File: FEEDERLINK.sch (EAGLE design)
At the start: 5 parts, among them J5 M02X5-SHROUDED

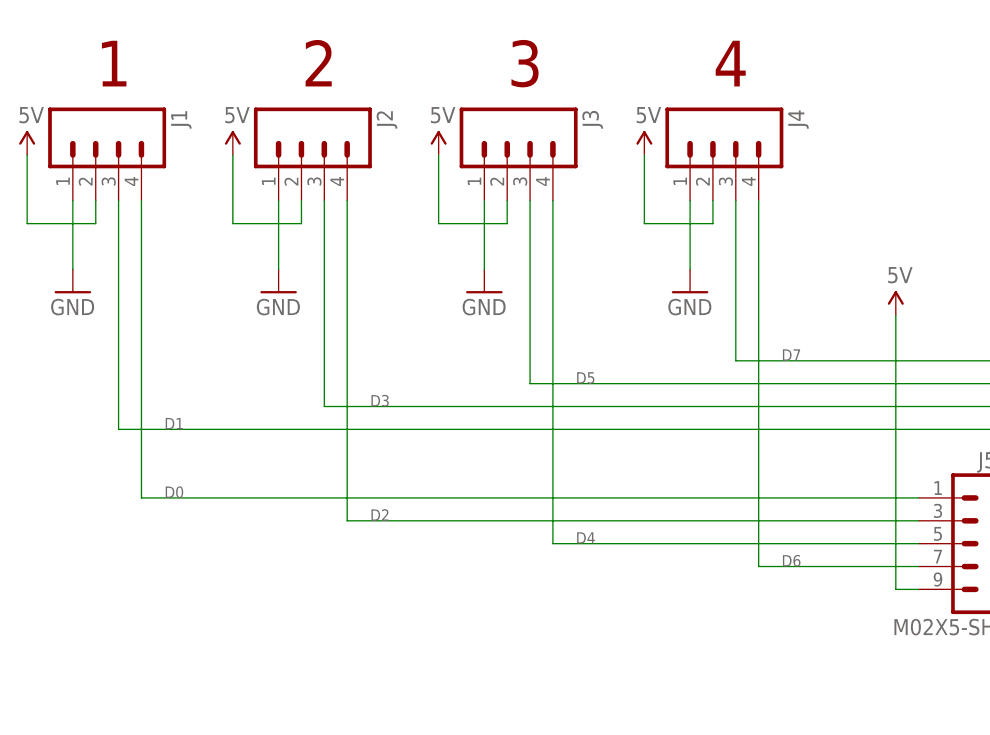
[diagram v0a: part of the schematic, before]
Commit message: Changed net names to match functions
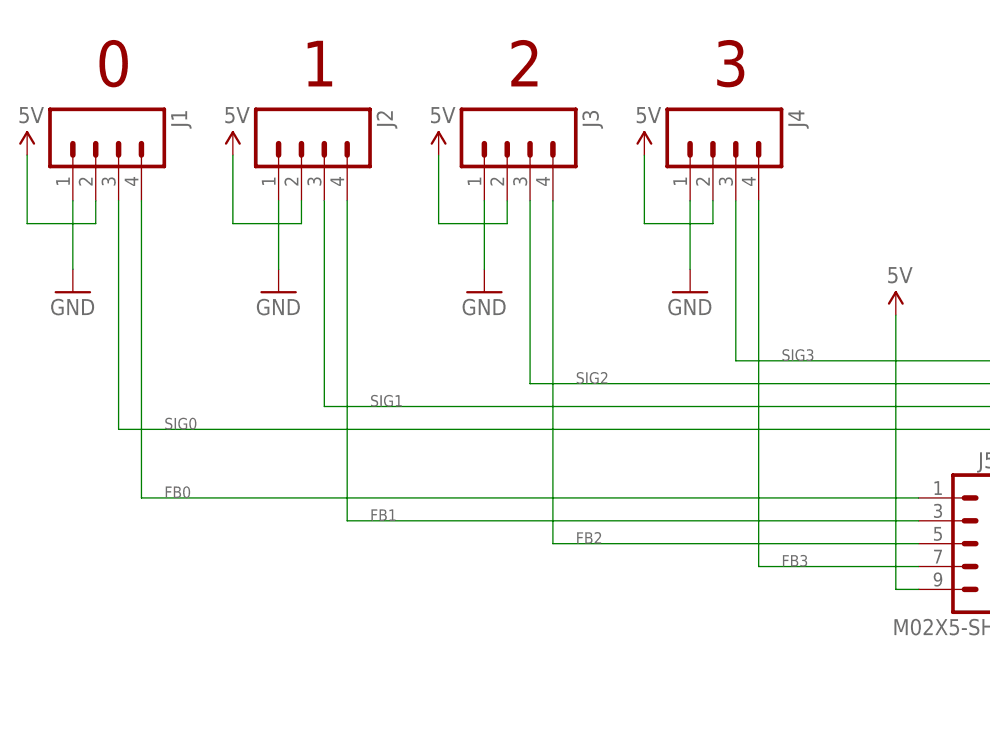
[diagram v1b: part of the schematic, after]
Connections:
- net D0 renamed FB0
- net D1 renamed SIG0
- net D2 renamed FB1
- net D3 renamed SIG1
- net D4 renamed FB2
- net D5 renamed SIG2
- net D6 renamed FB3
- net D7 renamed SIG3
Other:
- note added: "0"
- note removed: "4"
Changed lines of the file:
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@@
 <text x="134.366" y="6.35" size="1.778" layer="94">Released under the TAPR Open Hardware License: www.tapr.org/ohl</text>
 <text x="197.866" y="14.478" size="1.778" layer="94">www.superhouse.tv/fl</text>
-<text x="68.58" y="124.46" size="5.08" layer="94" ratio="12">1</text>
-<text x="91.44" y="124.46" size="5.08" layer="94" ratio="12">2</text>
-<text x="114.3" y="124.46" size="5.08" layer="94" ratio="12">3</text>
-<text x="137.16" y="124.46" size="5.08" layer="94" ratio="12">4</text>
+<text x="68.58" y="124.46" size="5.08" layer="94" ratio="12">0</text>
+<text x="91.44" y="124.46" size="5.08" layer="94" ratio="12">1</text>
+<text x="114.3" y="124.46" size="5.08" layer="94" ratio="12">2</text>
+<text x="137.16" y="124.46" size="5.08" layer="94" ratio="12">3</text>
 <frame x1="0" y1="0" x2="248.92" y2="185.42" columns="8" rows="5" layer="94"/>
 <frame x1="132.08" y1="12.7" x2="243.84" y2="25.4" columns="0" rows="0" layer="94" border-left="no" border-top="no" border-right="no" border-bottom="no"/>
@@
 </segment>
 </net>
-<net name="D0" class="0">
+<net name="FB0" class="0">
 <segment>
 <pinref part="J5" gate="G$1" pin="1"/>
@@
 </segment>
 </net>
-<net name="D1" class="0">
+<net name="SIG0" class="0">
 <segment>
 <pinref part="J5" gate="G$1" pin="2"/>
@@
 </segment>
 </net>
-<net name="D2" class="0">
+<net name="FB1" class="0">
 <segment>
 <pinref part="J5" gate="G$1" pin="3"/>
@@
 </segment>
 </net>
-<net name="D4" class="0">
+<net name="FB2" class="0">
 <segment>
 <pinref part="J5" gate="G$1" pin="5"/>
@@
 </segment>
 </net>
-<net name="D6" class="0">
+<net name="FB3" class="0">
 <segment>
 <pinref part="J5" gate="G$1" pin="7"/>
@@
 </segment>
 </net>
-<net name="D3" class="0">
+<net name="SIG1" class="0">
 <segment>
 <pinref part="J5" gate="G$1" pin="4"/>
@@
 </segment>
 </net>
-<net name="D5" class="0">
+<net name="SIG2" class="0">
 <segment>
 <pinref part="J5" gate="G$1" pin="6"/>
@@
 </segment>
 </net>
-<net name="D7" class="0">
+<net name="SIG3" class="0">
 <segment>
 <pinref part="J5" gate="G$1" pin="8"/>
